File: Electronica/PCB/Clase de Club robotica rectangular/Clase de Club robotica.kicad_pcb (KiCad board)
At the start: 2 copper layers, 17 parts, among them J1 Ultrasonico 1, J2 Screw_Terminal_01x02, J3 Ultrasonico 2, J4 Ultrasonico 3, J6 Screw_Terminal_01x02, SW1 SW_SPST, SW2 SW_Push

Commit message: Pcb En teoria Terminada y verificada por Prieto
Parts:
- J6: footprint Connector_PinSocket_2.54mm:PinSocket_1x02_P2.54mm_Vertical -> Connector_AMASS:AMASS_XT60-F_1x02_P7.20mm_Vertical
- moved R1 107.8 mm to (152.5, 165.3)
- moved D2 107.0 mm to (142.4, 161.0), turned to 180 degrees
- moved J6 103.6 mm to (134.2, 158.1), turned to -90 degrees
- moved SW1 98.6 mm to (142.5, 150.7), turned to 0 degrees
- moved U2 96.2 mm to (182.6, 171.4)
- moved D1 88.7 mm to (152.3, 144.8), turned to 180 degrees
- moved J2 69.8 mm to (199.5, 139.7), turned to -90 degrees
- moved U1 49.7 mm to (172.0, 141.5), turned to 180 degrees
- moved A1 25.0 mm to (146.1, 62.5)
- moved J1 25.0 mm to (176.6, 74.0)
- moved SensoresPISO1 25.0 mm to (182.0, 38.6)
- moved A2 25.0 mm to (174.3, 126.9)
- moved J3 25.0 mm to (176.8, 67.0)
- moved J4 25.0 mm to (181.4, 70.4)
- moved SensoresPISO2 25.0 mm to (162.5, 38.6)
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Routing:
- net GND: track 349.6 -> 576.0 mm, vias 0 -> 1
- net VIN: track 39.4 -> 206.0 mm
- net +5V: track 347.9 -> 410.7 mm, vias 0 -> 2
- net STEP DOWN: track 64.8 -> 93.9 mm
- net Earth: track 92.4 -> 66.1 mm
- net AIN1 MONSTER SHIELD: track 105.8 -> 96.2 mm
- net PWM B MONSTER SHIELD: track 90.5 -> 82.8 mm
- net Net-(D2-A): track 20.4 -> 13.7 mm
- net ECHO 1: track 17.9 -> 21.8 mm
- net TRIG 1: track 18.5 -> 22.4 mm
- net Net-(J2-Pin_1): track 9.80 -> 11.9 mm
- net Net-(J2-Pin_2): track 9.75 -> 10.6 mm
- net TRIG 3: track 31.1 -> 31.9 mm
- net Net-(D2-K): track 3.47 -> 4.26 mm

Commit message: .
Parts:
- moved U2 34.0 mm to (152.1, 156.3)
- moved SensoresPISO2 33.2 mm to (132.9, 23.5)
- moved A2 33.2 mm to (144.8, 111.8)
- moved D1 33.2 mm to (122.8, 129.7)
- moved J2 33.2 mm to (169.9, 124.5)
- moved J3 33.2 mm to (147.3, 51.9)
- moved J4 33.2 mm to (151.8, 55.2)
- moved R1 33.2 mm to (123.0, 150.2)
- moved U1 33.2 mm to (142.5, 126.3)
- moved A1 33.2 mm to (116.6, 47.3)
- moved D2 33.2 mm to (112.8, 145.9)
- moved J6 33.2 mm to (104.6, 143.0)
- moved SW1 33.2 mm to (113.0, 135.5)
- moved J1 33.2 mm to (147.1, 58.9)
- moved SW2 33.2 mm to (162.5, 37.0)
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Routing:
- net BIN 2 MONSTER SHIELD: track 16.9 -> 23.0 mm
- net PWM A MONSTER SHIELD: track 23.5 -> 19.2 mm
- net BIN 1 MONSTER SHIELD: track 23.5 -> 19.2 mm
- net GND: track 576.0 -> 573.6 mm, vias 1 -> 2
- net ECHO 1: track 21.8 -> 23.9 mm
- net VIN: track 206.0 -> 205.1 mm
- net STEP DOWN: track 93.9 -> 93.1 mm
- net (no net): vias 0 -> 2
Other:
- board text added: "EL BETO V1 AIDEN MAID PEREZ URIEL DYNER EITAN CHERNIAK"

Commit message: Me quiero cortar las bolas
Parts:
- A1, A2: moved to B.Cu
- moved A1 37.0 mm to (153.3, 42.6)
- moved A2 18.8 mm to (126.3, 108.1), turned to 0 degrees
- moved SensoresPISO1 3.93 mm to (151.8, 19.6)
- moved SensoresPISO3 3.93 mm to (127.8, 19.6)
- moved SensoresPISO2 3.93 mm to (132.2, 19.6)
- moved J3 3.93 mm to (146.6, 48.0)
- moved J4 3.93 mm to (151.2, 51.4)
- moved J1 3.44 mm to (146.4, 55.5)
- moved SW2 1.86 mm to (161.8, 35.3), turned to 180 degrees
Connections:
- A1 pad 10: TRIG 1 -> ECHO 3
- A1 pad 13: ECHO 3 -> TRIG 1
- A1 pad 14: TRIG 3 -> ECHO 1
- A1 pad 19: SENSOR DE PISO 1 -> SENSOR DE PISO 3
- A1 pad 22: BOTON  -> AIN1 MONSTER SHIELD
- A1 pad 25: AIN1 MONSTER SHIELD -> BOTON 
- A1 pad 26: SENSOR DE PISO 3 -> SENSOR DE PISO 1
- A1 pad 9: ECHO 1 -> TRIG 3
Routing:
- net GND: track 573.6 -> 124.6 mm, vias 2 -> 0
- net +5V: track 410.7 -> 70.2 mm, vias 2 -> 0
- net VIN: track 205.1 -> 0.00 mm
- net AIN1 MONSTER SHIELD: track 96.2 -> 0.00 mm
- net AIN2 MONSTER SHIELD: track 91.7 -> 0.00 mm
- net PWM B MONSTER SHIELD: track 82.8 -> 0.00 mm
- net TRIG 2: track 4.65 -> 30.6 mm
- net BIN 2 MONSTER SHIELD: track 23.0 -> 0.00 mm
- net BIN 1 MONSTER SHIELD: track 19.2 -> 0.00 mm
- net PWM A MONSTER SHIELD: track 19.2 -> 0.00 mm
- net ECHO 3: track 48.3 -> 30.0 mm
- net ECHO 2: track 4.65 -> 22.9 mm
- net TRIG 1: track 22.4 -> 33.6 mm
- net SENSOR DE PISO 2: track 9.18 -> 19.7 mm
- net ECHO 1: track 23.9 -> 33.9 mm
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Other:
- board text removed: "EL BETO V1 AIDEN MAID PEREZ URIEL DYNER EITAN CHERNIAK"

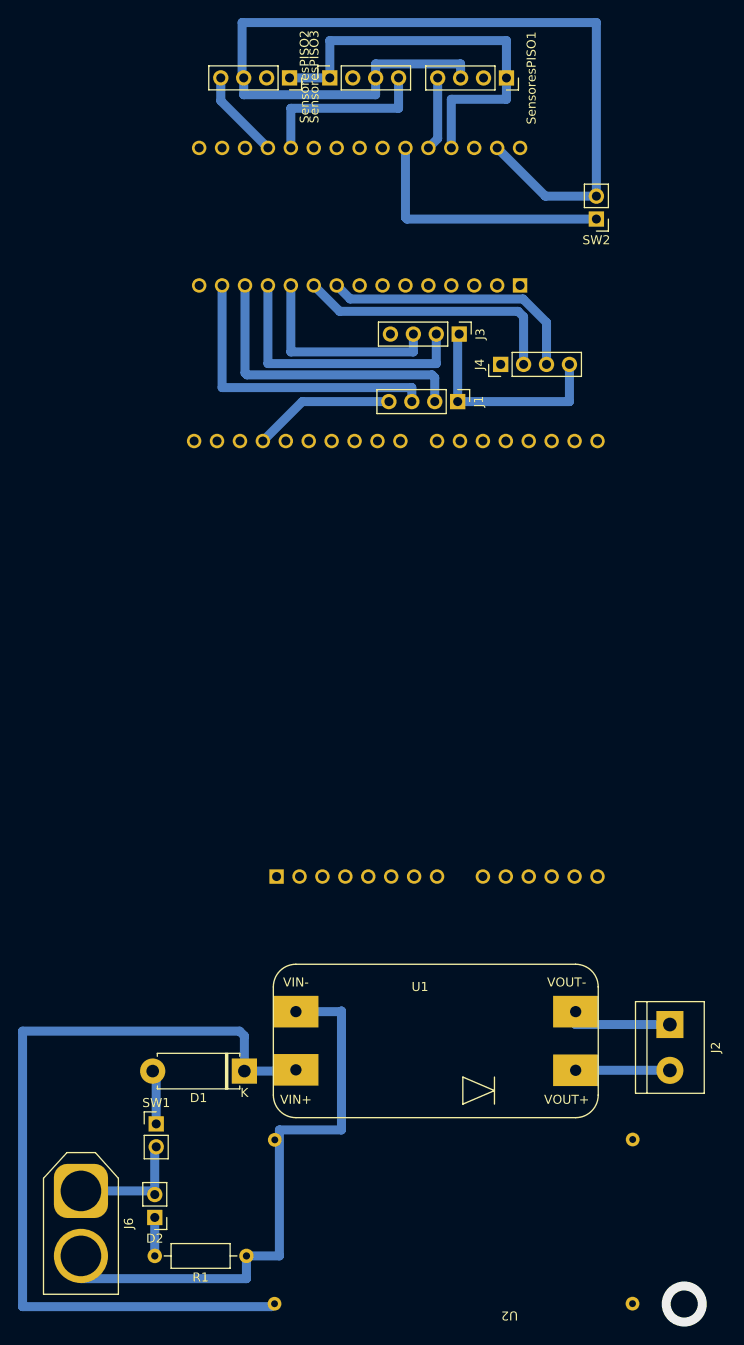
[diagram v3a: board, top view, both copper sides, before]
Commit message: Placa corregida sin placa de botones
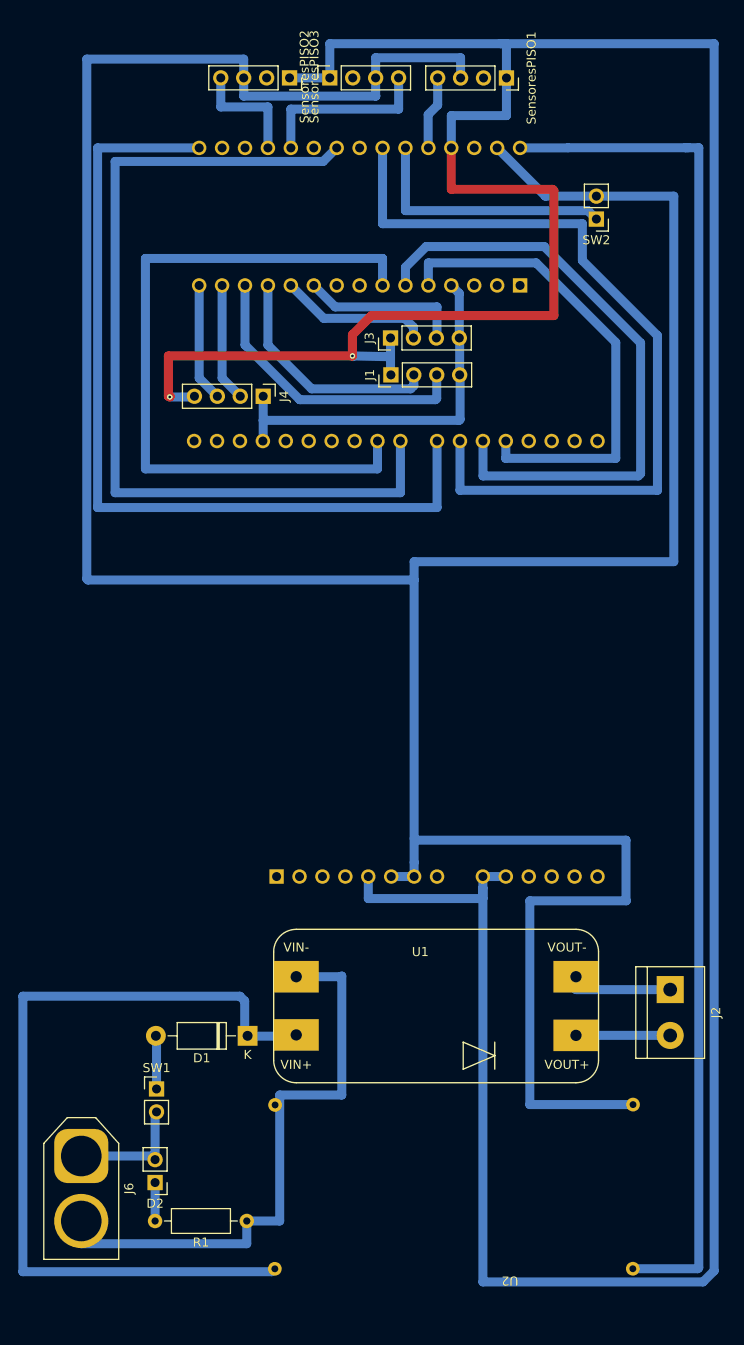
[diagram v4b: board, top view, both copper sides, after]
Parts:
- D1: value D -> 1N4007; footprint Diode_THT:D_5W_P10.16mm_Horizontal -> Diode_THT:D_DO-41_SOD81_P10.16mm_Horizontal
- moved J4 26.6 mm to (124.8, 54.9), turned to -90 degrees
- moved J1 7.97 mm to (139.0, 52.5), turned to 90 degrees
- moved J3 7.62 mm to (138.9, 48.5), turned to 90 degrees
- moved D1 3.93 mm to (123.1, 125.8)
- moved D2 3.87 mm to (112.9, 142.0)
- moved J2 3.87 mm to (169.9, 120.7)
- moved J6 3.87 mm to (104.7, 139.1)
- moved SW1 3.87 mm to (113.0, 131.7)
- moved U2 3.87 mm to (152.2, 152.4)
- moved U1 3.87 mm to (142.5, 122.5)
- moved R1 3.87 mm to (123.0, 146.3)
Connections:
- A1 pad 10: ECHO 3 -> ECHO 2
- A1 pad 11: ECHO 2 -> TRIG 2
- A1 pad 12: TRIG 2 -> TRIG 1
- A1 pad 13: TRIG 1 -> ECHO 1
- A1 pad 14: ECHO 1 -> ECHO 3
- A1 pad 15: unconnected-(A1-D12-Pad15) -> TRIG 3
- A1 pad 16: AIN2 MONSTER SHIELD -> AIN1 MONSTER SHIELD
- A1 pad 22: AIN1 MONSTER SHIELD -> AIN2 MONSTER SHIELD
- A1 pad 9: TRIG 3 -> unconnected-(A1-D6-Pad9)
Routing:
- net +5V: track 70.2 -> 386.9 mm, vias 0 -> 2
- net GND: track 124.6 -> 391.5 mm
- net VIN: track 0.00 -> 151.6 mm
- net AIN2 MONSTER SHIELD: track 0.00 -> 99.2 mm
- net AIN1 MONSTER SHIELD: track 0.00 -> 96.1 mm
- net PWM B MONSTER SHIELD: track 0.00 -> 90.9 mm
- net BIN 2 MONSTER SHIELD: track 0.00 -> 81.4 mm
- net PWM A MONSTER SHIELD: track 0.00 -> 69.4 mm
- net BIN 1 MONSTER SHIELD: track 0.00 -> 53.9 mm
- net ECHO 3: track 30.0 -> 13.1 mm
- net TRIG 3: track 29.6 -> 13.1 mm
- net TRIG 2: track 30.6 -> 16.7 mm
- net TRIG 1: track 33.6 -> 26.1 mm
- net ECHO 2: track 22.9 -> 18.1 mm
- net SENSOR DE PISO 3: track 9.92 -> 13.0 mm
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
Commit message: PCB de botones
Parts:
- added D3: LED, LED_THT:LED_D5.0mm, F.Cu at (223.5, 96.2)
- added D4: LED, LED_THT:LED_D5.0mm, F.Cu at (223.7, 82.7)
- added D5: LED, LED_THT:LED_D5.0mm, F.Cu at (223.6, 89.4)
- added D6: LED, LED_THT:LED_D5.0mm, F.Cu at (223.7, 75.8)
- added D7: LED, LED_THT:LED_D5.0mm, F.Cu at (223.8, 68.6)
- added J7: Conn_02x05_Counter_Clockwise, Connector_IDC:IDC-Header_2x05_P2.54mm_Vertical, F.Cu at (210.3, 75.1)
- added R2: 660, Resistor_THT:R_Axial_DIN0207_L6.3mm_D2.5mm_P10.16mm_Horizontal, F.Cu at (242.8, 89.6)
- added R3: 220, Resistor_THT:R_Axial_DIN0207_L6.3mm_D2.5mm_P10.16mm_Horizontal, F.Cu at (242.8, 81.6)
- added R4: 220, Resistor_THT:R_Axial_DIN0207_L6.3mm_D2.5mm_P10.16mm_Horizontal, F.Cu at (242.7, 85.2)
- added R5: 220, Resistor_THT:R_Axial_DIN0207_L6.3mm_D2.5mm_P10.16mm_Horizontal, F.Cu at (242.8, 77.5)
- added R6: 220, Resistor_THT:R_Axial_DIN0207_L6.3mm_D2.5mm_P10.16mm_Horizontal, F.Cu at (243.0, 71.9)
- added SW3: SW_SPST, Button_Switch_THT:SW_Slide_SPDT_Angled_CK_OS102011MA1Q, F.Cu at (210.1, 93.7)
- added SW4: SW_Push, Button_Switch_THT:SW_PUSH_6mm, F.Cu at (247.6, 72.9)
- added SW5: SW_Push, Button_Switch_THT:SW_PUSH_6mm, F.Cu at (247.6, 81.4)
- J6: footprint Connector_AMASS:AMASS_XT60-F_1x02_P7.20mm_Vertical -> Connector_AMASS:AMASS_XT60-M_1x02_P7.20mm_Vertical
- moved J1 83.0 mm to (56.0, 50.9)
- moved A1 83.0 mm to (70.4, 41.0)
- moved A2 83.0 mm to (43.4, 106.5)
- moved D1 83.0 mm to (40.2, 124.1)
- moved D2 83.0 mm to (29.9, 140.4)
- moved J2 83.0 mm to (87.0, 119.0)
- moved J4 83.0 mm to (41.9, 53.3)
- moved J6 83.0 mm to (21.7, 137.4)
- moved SensoresPISO3 83.0 mm to (44.8, 18.0)
- moved U1 83.0 mm to (59.5, 120.8)
- moved U2 83.0 mm to (69.2, 150.8)
- moved J3 83.0 mm to (56.0, 46.8)
- moved R1 83.0 mm to (40.1, 144.7)
- moved SW1 83.0 mm to (30.1, 130.0)
- moved SW2 83.0 mm to (78.8, 33.6)
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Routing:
- net Earth: track 66.1 -> 160.0 mm
- net Net-(J7-Pin_5): track 0.00 -> 92.2 mm
- net GND: track 391.5 -> 459.6 mm
- net Net-(J7-Pin_6): track 0.00 -> 67.7 mm
- net Net-(D5-A): track 0.00 -> 53.2 mm
- net Net-(D3-A): track 0.00 -> 33.9 mm
- net Net-(D3-K): track 0.00 -> 27.3 mm
- net Net-(D7-A): track 0.00 -> 26.3 mm
- net Net-(D5-K): track 0.00 -> 21.2 mm
- net Net-(D7-K): track 0.00 -> 12.3 mm
- net Net-(D6-K): track 0.00 -> 9.69 mm
- net Net-(J7-Pin_10): track 0.00 -> 9.52 mm
- net Net-(D4-K): track 0.00 -> 9.36 mm
- net Net-(D6-A): track 0.00 -> 9.07 mm
- net Net-(D4-A): track 0.00 -> 8.37 mm
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
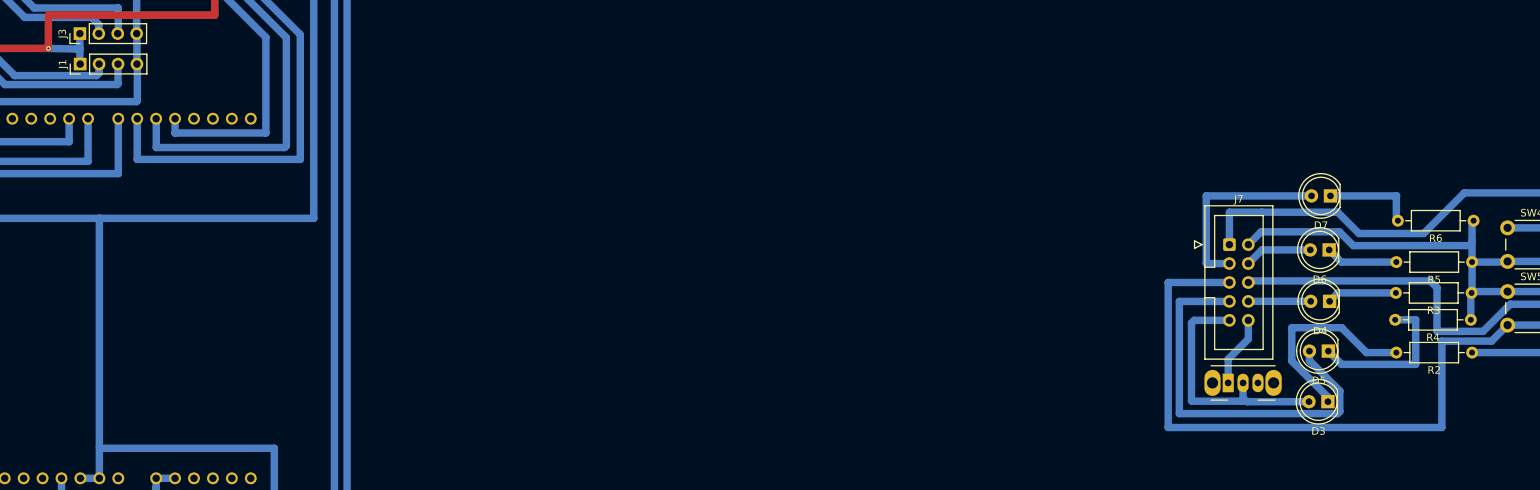
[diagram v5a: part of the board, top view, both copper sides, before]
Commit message: Pcb de botones
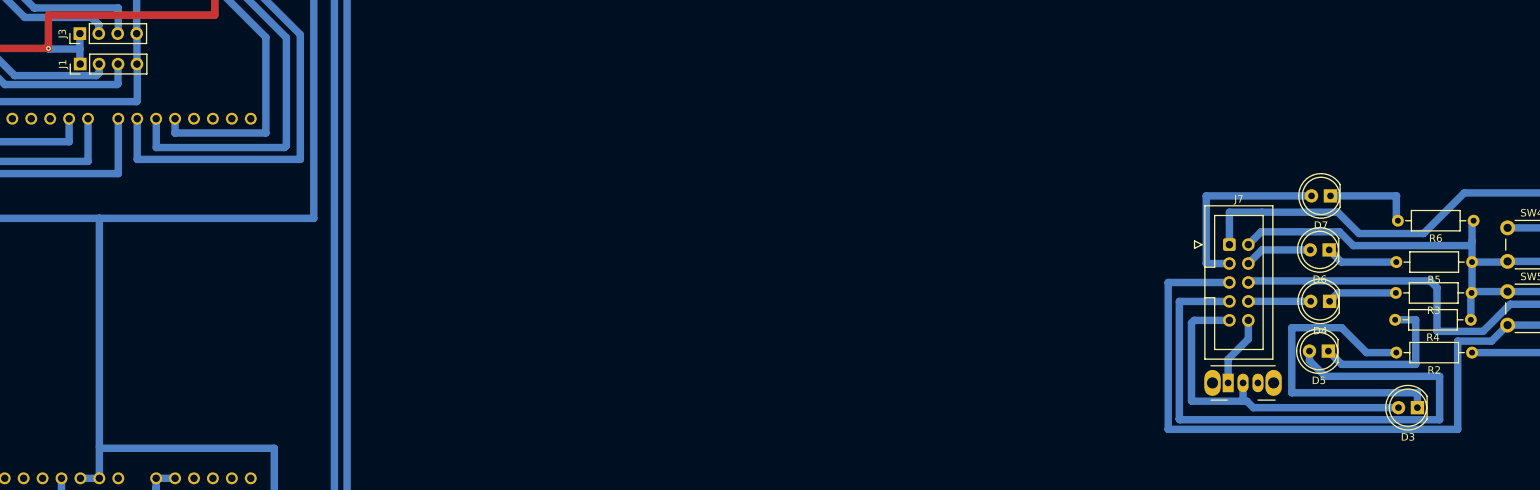
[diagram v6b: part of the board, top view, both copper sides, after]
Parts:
- moved D3 12.0 mm to (235.5, 97.0)
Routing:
- net Net-(D5-A): track 53.2 -> 82.9 mm
- net Net-(D3-K): track 27.3 -> 43.0 mm
- net Net-(D3-A): track 33.9 -> 46.3 mm
- net Net-(J7-Pin_5): track 92.2 -> 92.7 mm
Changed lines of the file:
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@@
 	(footprint "LED_THT:LED_D5.0mm"
 		(layer "F.Cu")
-		(at 223.49 96.2 180)
+		(at 235.5 97 180)
 		(descr "LED, diameter 5.0mm, 2 pins, http://cdn-reichelt.de/documents/datenblatt/A500/LL-504BC2E-009.pdf")
 		(tags "LED diameter 5.0mm 2 pins")
@@
 	)
 	(segment
+		(start 51.78 48.79)
+		(end 51.86 48.87)
+		(width 1)
+		(layer "B.Cu")
+		(net 20)
+	)
+	(segment
 		(start 56 48.87)
 		(end 56 50.85)
@@
 	)
 	(segment
+		(start 51.86 48.87)
+		(end 55.55 48.87)
+		(width 1)
+		(layer "B.Cu")
+		(net 20)
+	)
+	(segment
 		(start 62.735 22.16)
 		(end 68.845 22.16)
@@
 	)
 	(segment
-		(start 56 48.87)
-		(end 55.55 48.87)
-		(width 1)
-		(layer "B.Cu")
-		(net 20)
-	)
-	(segment
 		(start 66.235 107.74)
 		(end 66.235 106.48)
@@
 	)
 	(segment
-		(start 55.55 48.87)
-		(end 51.78 48.79)
-		(width 1)
-		(layer "B.Cu")
-		(net 20)
-	)
-	(segment
 		(start 68.845 22.16)
 		(end 68.845 17.99)
@@
 	)
 	(segment
-		(start 212.68 96.2)
-		(end 220.95 96.2)
+		(start 205.54 85.28)
+		(end 210.27 85.28)
 		(width 1)
 		(layer "B.Cu")
@@
 	)
 	(segment
-		(start 205.54 85.28)
-		(end 210.27 85.28)
+		(start 213.48 97)
+		(end 212.61 96.13)
 		(width 1)
 		(layer "B.Cu")
@@
 	)
 	(segment
-		(start 212.61 96.13)
-		(end 212.68 96.2)
+		(start 205.18 96.08)
+		(end 205.18 85.64)
 		(width 1)
 		(layer "B.Cu")
@@
 	)
 	(segment
-		(start 212.1 96.13)
-		(end 212.61 96.13)
+		(start 232.96 97)
+		(end 213.48 97)
 		(width 1)
 		(layer "B.Cu")
@@
 	)
 	(segment
-		(start 205.18 96.08)
-		(end 205.18 85.64)
+		(start 205.23 96.13)
+		(end 205.18 96.08)
 		(width 1)
 		(layer "B.Cu")
@@
 	)
 	(segment
-		(start 205.23 96.13)
-		(end 205.18 96.08)
+		(start 212.1 96.13)
+		(end 212.61 96.13)
 		(width 1)
 		(layer "B.Cu")
@@
 	)
 	(segment
-		(start 218.64 90.73)
-		(end 223.49 95.58)
+		(start 225.332032 86.272032)
+		(end 218.64 86.272032)
 		(width 1)
 		(layer "B.Cu")
@@
 	)
 	(segment
-		(start 218.64 86.272032)
-		(end 218.64 90.73)
+		(start 218.64 95)
+		(end 235.5 95)
 		(width 1)
 		(layer "B.Cu")
@@
 	)
 	(segment
-		(start 232.67 89.61)
-		(end 228.67 89.61)
+		(start 228.67 89.61)
+		(end 225.332032 86.272032)
 		(width 1)
 		(layer "B.Cu")
@@
 	)
 	(segment
-		(start 228.67 89.61)
-		(end 225.332032 86.272032)
+		(start 232.67 89.61)
+		(end 228.67 89.61)
 		(width 1)
 		(layer "B.Cu")
@@
 	)
 	(segment
-		(start 225.332032 86.272032)
-		(end 218.64 86.272032)
+		(start 235.5 95)
+		(end 235.5 97)
 		(width 1)
 		(layer "B.Cu")
@@
 	)
 	(segment
-		(start 223.49 95.58)
-		(end 223.49 96.2)
+		(start 218.64 86.272032)
+		(end 218.64 95)
 		(width 1)
 		(layer "B.Cu")
@@
 	)
 	(segment
-		(start 224.8 97.8)
-		(end 203.55 97.8)
+		(start 223.117208 92.79)
+		(end 238.48 92.79)
 		(width 1)
 		(layer "B.Cu")
@@
 	)
 	(segment
-		(start 203.55 97.8)
+		(start 203.55 98.53)
 		(end 203.55 82.74)
 		(width 1)
@@
 	)
 	(segment
-		(start 221.01 89.41)
-		(end 221.01 90.682792)
+		(start 238.48 98.62)
+		(end 203.62 98.62)
 		(width 1)
 		(layer "B.Cu")
@@
 	)
 	(segment
-		(start 203.55 82.74)
-		(end 210.27 82.74)
+		(start 203.54 98.54)
+		(end 203.55 98.53)
 		(width 1)
 		(layer "B.Cu")
@@
 	)
 	(segment
-		(start 225.09 94.762792)
-		(end 225.09 97.51)
+		(start 221.01 90.682792)
+		(end 223.117208 92.79)
 		(width 1)
 		(layer "B.Cu")
@@
 	)
 	(segment
-		(start 221.01 90.682792)
-		(end 225.09 94.762792)
+		(start 221.01 89.41)
+		(end 221.01 90.682792)
+		(width 1)
+		(layer "B.Cu")
+		(net 65)
+	)
+	(segment
+		(start 203.62 98.62)
+		(end 203.54 98.54)
 		(width 1)
 		(layer "B.Cu")
@@
 	)
 	(segment
-		(start 225.09 97.51)
-		(end 224.8 97.8)
+		(start 203.55 82.74)
+		(end 210.27 82.74)
+		(width 1)
+		(layer "B.Cu")
+		(net 65)
+	)
+	(segment
+		(start 238.48 92.79)
+		(end 238.48 98.62)
 		(width 1)
 		(layer "B.Cu")
@@
 	)
 	(segment
-		(start 202.05 99.66)
-		(end 238.78 99.66)
+		(start 202.05 99.91)
+		(end 240.91 99.91)
 		(width 1)
 		(layer "B.Cu")
@@
 	)
 	(segment
-		(start 202.05 80.2)
-		(end 202.05 99.66)
+		(start 240.91 99.91)
+		(end 240.91 88.07)
 		(width 1)
 		(layer "B.Cu")
@@
 	)
 	(segment
-		(start 245.45 88.07)
-		(end 247.6 85.92)
+		(start 210.27 80.2)
+		(end 202.05 80.2)
 		(width 1)
 		(layer "B.Cu")
@@
 	)
 	(segment
-		(start 238.78 88.07)
-		(end 245.45 88.07)
+		(start 202.05 80.2)
+		(end 202.05 99.91)
 		(width 1)
 		(layer "B.Cu")
@@
 	)
 	(segment
-		(start 238.78 99.66)
-		(end 238.78 88.07)
+		(start 240.91 88.07)
+		(end 245.45 88.07)
 		(width 1)
 		(layer "B.Cu")
@@
 	)
 	(segment
-		(start 210.27 80.2)
-		(end 202.05 80.2)
+		(start 254.1 85.92)
+		(end 247.6 85.92)
 		(width 1)
 		(layer "B.Cu")
@@
 	)
 	(segment
-		(start 254.1 85.92)
+		(start 245.45 88.07)
 		(end 247.6 85.92)
 		(width 1)

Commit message: ?
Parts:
- moved SW4 132.4 mm to (115.3, 69.6), turned to 90 degrees
- moved R6 128.7 mm to (114.3, 74.2), turned to -90 degrees
- moved SW5 124.3 mm to (123.8, 69.6), turned to 90 degrees
- moved R5 123.0 mm to (119.9, 74.4), turned to -90 degrees
- moved R3 119.0 mm to (124.0, 74.4), turned to -90 degrees
- moved R4 115.5 mm to (127.6, 74.5), turned to -90 degrees
- moved D7 115.5 mm to (111.0, 93.4), turned to -90 degrees
- moved R2 111.8 mm to (132.0, 74.4), turned to -90 degrees
- moved D6 106.9 mm to (118.2, 93.5), turned to -90 degrees
- moved D4 99.2 mm to (125.2, 93.5), turned to -90 degrees
- moved J7 98.0 mm to (117.5, 106.9), turned to 90 degrees
- moved D3 97.3 mm to (139.4, 81.7), turned to -90 degrees
- moved D5 91.8 mm to (131.8, 93.7), turned to -90 degrees
- moved SW3 75.2 mm to (136.1, 107.1), turned to 90 degrees

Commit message: PCB Botones
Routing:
- net VIN: track 151.6 -> 149.7 mm
- net BIN 1 MONSTER SHIELD: track 53.9 -> 54.6 mm
